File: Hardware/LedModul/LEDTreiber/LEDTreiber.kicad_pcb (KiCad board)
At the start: 2 copper layers, 16.8 x 16.8 mm, 15 parts, among them J1 Conn_01x01_Pin, J2 Conn_01x01_Pin, J3 Conn_01x01_Pin, J4 Conn_01x01_Pin, J5 Conn_01x01_Pin, U1 TPS92200DxRXL, U2 TVS2700DRV

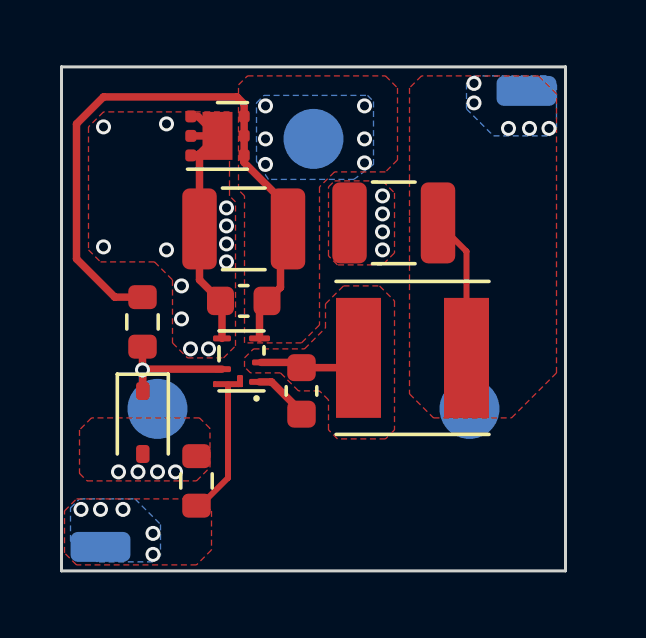
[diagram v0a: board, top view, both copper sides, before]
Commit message: PogoPin pcb added
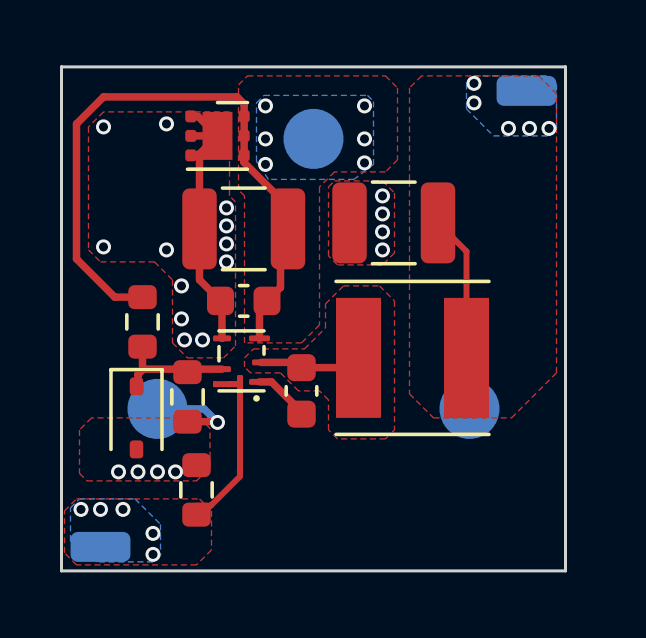
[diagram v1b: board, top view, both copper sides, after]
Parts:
- added R3: 1k, Resistor_SMD:R_0603_1608Metric, F.Cu at (74.2, 134.2)
- R1: value 100k -> 1M
- moved R2 0.30 mm to (74.5, 137.3)
- moved D1 0.26 mm to (72.5, 134.9)
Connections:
- D1 pad 1: /PWM -> Net-(D1-K)
- R1 pad 2: /PWM -> Net-(D1-K)
- U1 pad 5: /PWM -> Net-(D1-K)
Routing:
- net Net-(D1-K): track 0.00 -> 4.08 mm
- net /PWM: track 5.68 -> 3.90 mm
- net /LED-: track 4.56 -> 5.33 mm

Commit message: added Pcb name and version to silkscreen
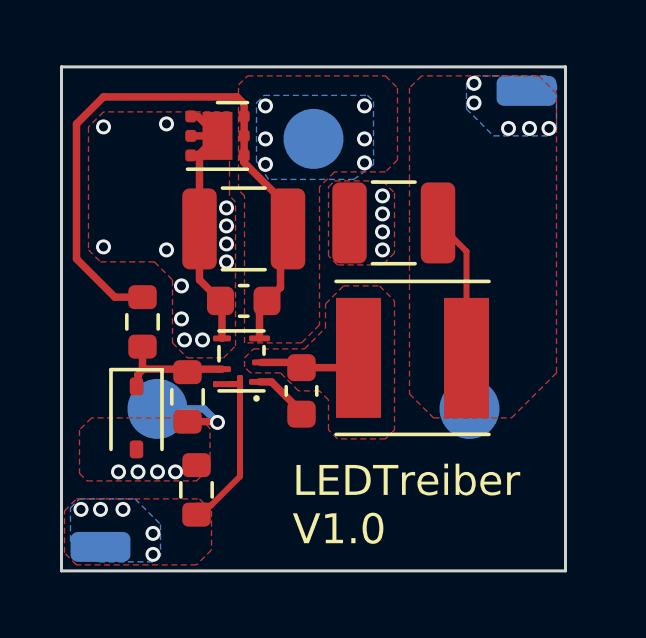
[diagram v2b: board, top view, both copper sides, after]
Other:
- board text added: "LEDTreiber V1.0"
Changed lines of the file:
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@@
+    (effects (font (size 1 1) (thickness 0.15)) (justify left bottom mirror))
+  )
+  (gr_text "LEDTreiber \nV1.0" (at 73.5 123.7 90) (layer "B.SilkS")
     (effects (font (size 1 1) (thickness 0.15)) (justify left bottom mirror))
   )
@@
     (effects (font (size 1 1) (thickness 0.15)) (justify left bottom mirror))
   )
+  (gr_text "LEDTreiber \nV1.0" (at 77.7 139.2) (layer "F.SilkS")
+    (effects (font (size 1 1) (thickness 0.15)) (justify left bottom))
+  )
   (dimension (type aligned) (layer "Dwgs.User")

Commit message: V1.1
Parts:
- J1, J2: footprint Bergi:Solderpad_1x2 -> Connector_PinHeader_2.54mm:PinHeader_1x01_P2.54mm_Vertical; moved to F.Cu
- moved J1 0.55 mm to (85.5, 124.5), turned to 0 degrees
- moved J2 0.55 mm to (71.3, 138.7), turned to 0 degrees
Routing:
- net /LED-: vias 5 -> 3
- net /LED+: vias 5 -> 3
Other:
- board text added: "LEDTreiber V1.1"
- board text removed: "LEDTreiber V1.0"
